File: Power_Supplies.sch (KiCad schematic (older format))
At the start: 70 parts

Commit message: Rick's changes - April 19
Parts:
- removed L?: L_22uH_2.6A_42mOhm_SMT, F_Inductors:L-Bourns-SRU1048-series, symbol OpenVent:L_22uH_2.6A_42mOhm_SMT
- added L?: L_22uH_2.6A_42mOhm_SMT, F_Inductors:L-Bourns-SRU1048-series, symbol OpenVent:L_22uH_2.6A_42mOhm_SMT
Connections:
- net +5V: now also L?.2; no longer L?.1
- net FAN_DRIVE: now also J?.3 (Pin_3); no longer J?.4 (Pin_4)
- net GND: now also D?.2 (CATHODE)
- net PWR_EN: no longer U?.5 (EN)
- net VBUS: now also J?.4 (Pin_4); no longer J?.3 (Pin_3)
- net VDC: now also D2.1 (ANODE), D?.1 (ANODE)
- net V_MAIN: now also L?.2
- net at D2.2 (CATHODE): now also R?.2
- net at D?.1 (ANODE): now also R?.2
- net at C?.1, C?.1, FB?.2: now also L?.1; no longer L?.2
- net at C?.1, C?.1, FB?.2: now also L?.1
- net at R?.1: now also D?.2 (CATHODE)
- net VIN_FAIL_FPGA renamed VIN_FAIL_F
- net VIN_FAIL_MCU renamed VIN_FAIL_M
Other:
- note added: "Add 5V Sensor Power Supply"
- note added: "Add Power Supervisor\nto 7.5V_IN to enable\nlinear regulators"
- note removed: "(Use only for status check of external power supply.)"
- note removed: "(VIN_LIMITED is connected to input 12V through a 1K resistor.)"
- note removed: "Add 5V Sensor Power \nSupply with prefiltering"
- note removed: "FAN DRIVE NEEDS TO BE GENERATED BY FPGA - ANY VOLTAGE\n"
- note removed: "SW_HOME, SW_END, SW_BACKUP\nare off-board microswitches"
- note removed: "Swap VBATT and FAN_DRIVE here and Power board to \nprevent serious damage if cable is installed backwards"
- moved on the sheet: C?, D2, D?, FB?, L?, M?, Q?, R14, R?, U?

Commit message: Annotation has been done
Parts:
- gave numbers to parts that had none: 66
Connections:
- net VMEM: now also D17.6 (K1;A2); no longer D17.3 (A3;K4)
- net V_MAIN: now also D16.3 (A3;K4); no longer D16.6 (K1;A2)
- net at C103.2, U23.4 (VIN), U23.5 (EN): now also D16.5 (K3), D17.2 (K2); no longer D16.2 (K2), D17.5 (K3)

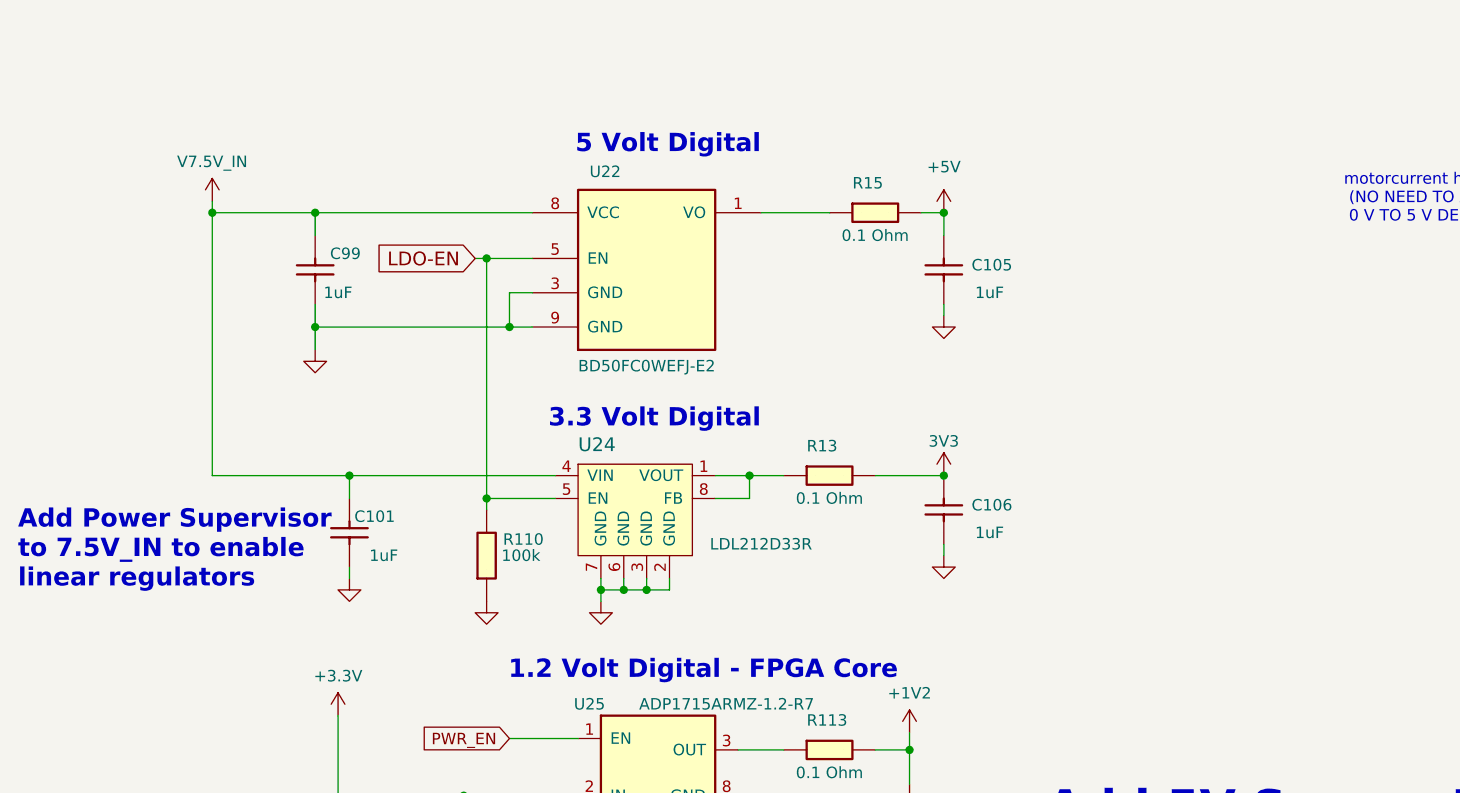
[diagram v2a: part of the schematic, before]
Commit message: Update Power_Supplies.sch
PoR for 7.5V added
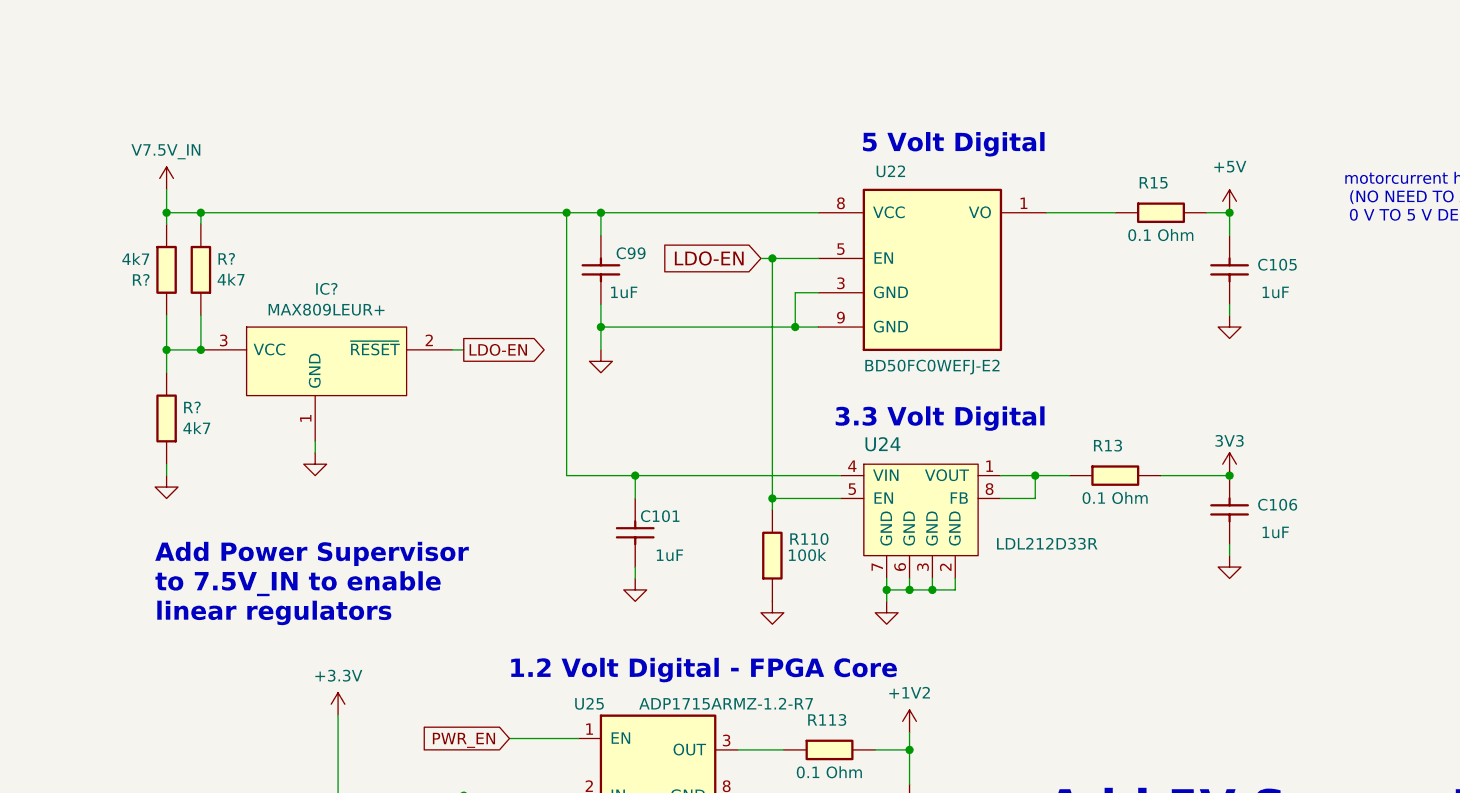
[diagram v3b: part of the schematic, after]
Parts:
- added IC?: MAX809LEUR+, SOT95P237X112-3N, symbol OpenVent:MAX809LEUR+
- added R? (x3): 4.7K_±0.1%_1_6W_±25ppm_℃_0603_High_Precision_&_Lo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, symbol OpenVent:4.7K_±0.1%_1_6W_±25ppm_℃_0603_High_Precision_&_Low_TCR_SMD_Resistors_R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
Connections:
- net +5V: now also R?.1, R?.2
- net GND: now also IC?.1 (GND), R?.1
- net LDO-EN: now also IC?.2 (~RESET)
- new net: IC?.3 (VCC), R?.1, R?.2, R?.2
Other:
- moved on the sheet: C101, C105, C106, C99, R110, R13, R15, U22, U24

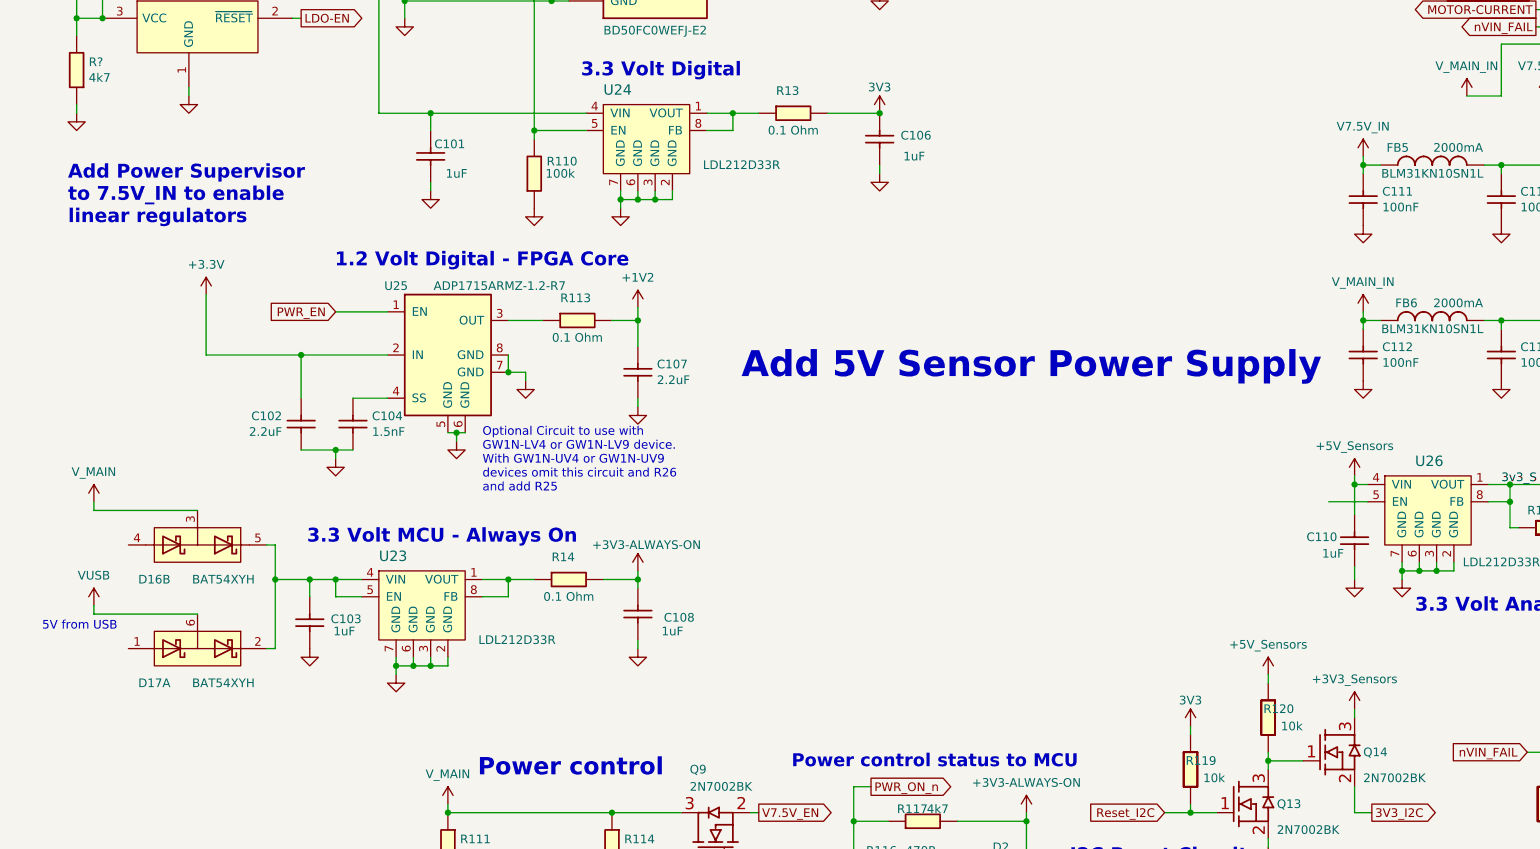
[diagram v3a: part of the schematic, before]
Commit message: Update Power_Supplies.sch
5V analog added
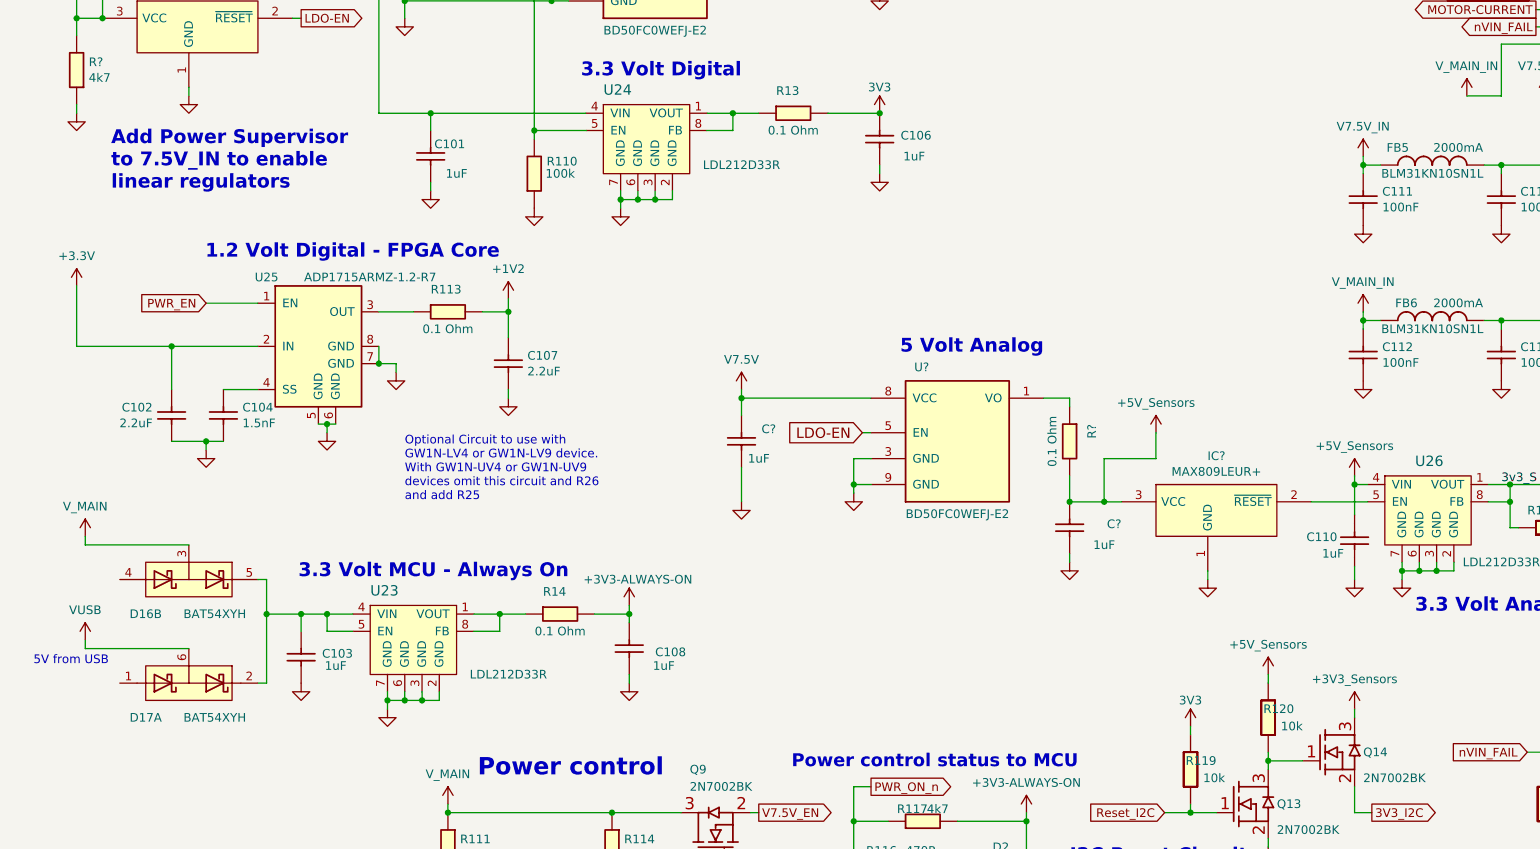
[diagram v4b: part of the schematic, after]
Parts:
- added C? (x2): 1uF_0603_Ceramic_Capacitor,_10%,_50V,_X5R, Capacitor_SMD:C_0603_1608Metric, symbol OpenVent:1uF_0603_Ceramic_Capacitor,_10%,_50V,_X5R
- added IC?: MAX809LEUR+, SOT95P237X112-3N, symbol OpenVent:MAX809LEUR+
- added R?: 0R1_0603_Chip_Resistor,_1%,_0.1W, Resistor_SMD:R_0603_1608Metric, symbol OpenVent:0R1_0603_Chip_Resistor,_1%,_0.1W
- added U?: BD50FC0WEFJ-E2, Package_SO:HSOP-8-1EP_3.9x4.9mm_P1.27mm_EP2.41x3.1mm_ThermalVias, symbol OpenVent:BD50FC0WEFJ-E2
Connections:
- net +5V: now also C?.2, C?.2, IC?.3 (VCC), R?.2, U?.8 (VCC)
- net GND: now also C?.1, C?.1, IC?.1 (GND), U?.3 (GND), U?.9 (GND)
- net LDO-EN: now also U?.5 (EN)
- net at U26.5 (EN): now also IC?.2 (~RESET)
- new net: R?.1, U?.1 (VO)
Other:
- note added: "5 Volt Analog"
- note removed: "Add 5V Sensor Power Supply"
- moved on the sheet: C102, C103, C104, C107, C108, D16B, D17A, R113, R14, U23, U25

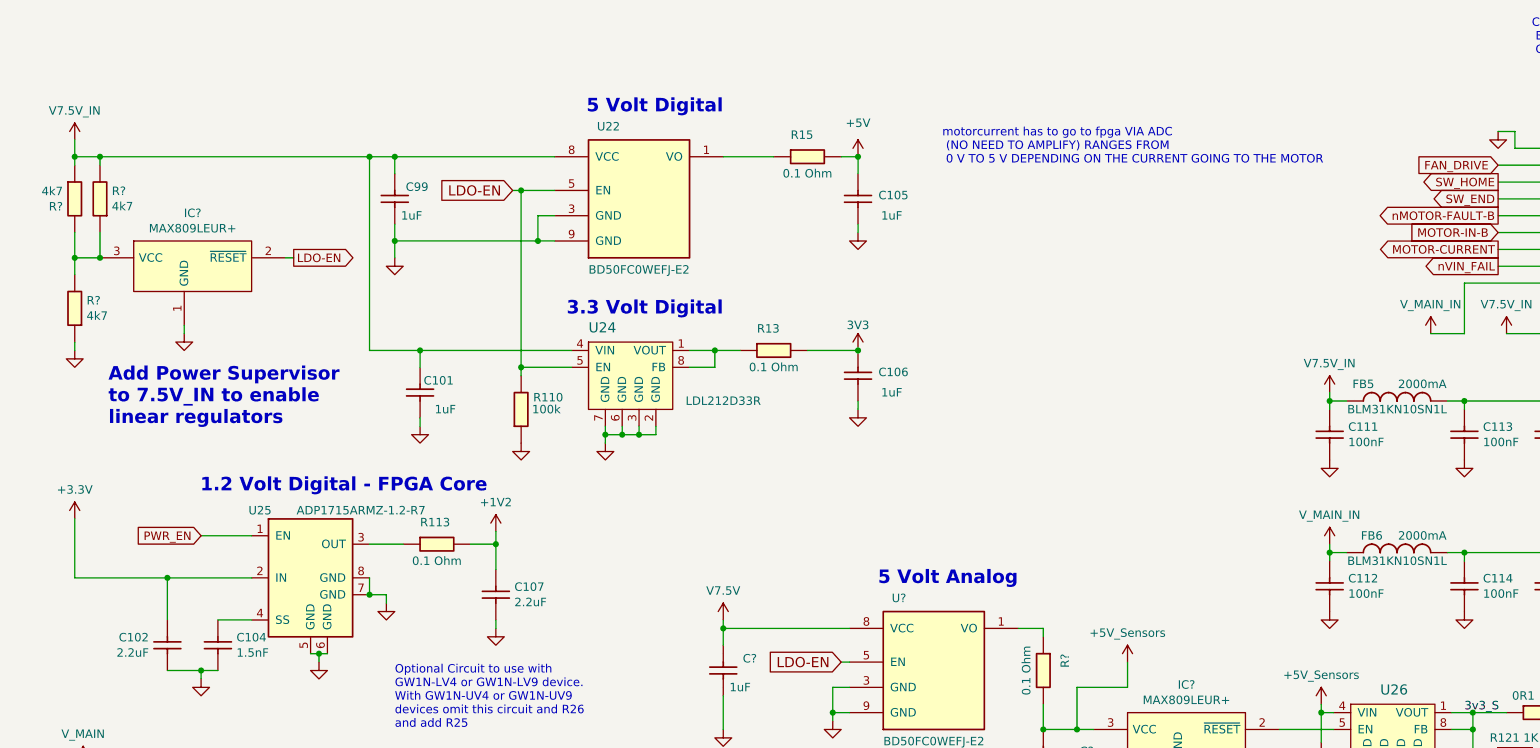
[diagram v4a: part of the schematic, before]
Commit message: Update Power_Supplies.sch
3.3v regulator with soft-start added
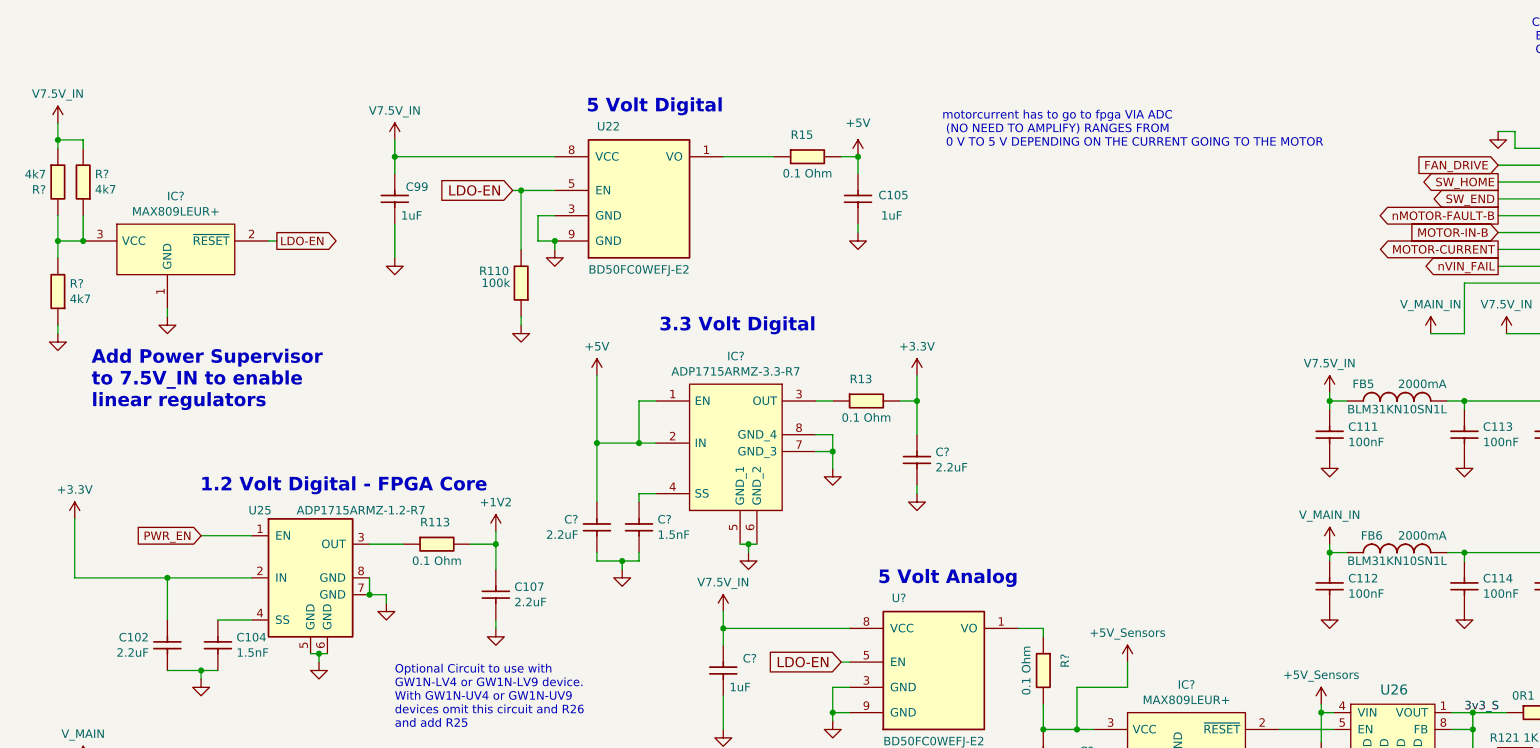
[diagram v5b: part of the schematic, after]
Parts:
- removed C101, C106: 1uF_0603_Ceramic_Capacitor,_10%,_50V,_X5R, Capacitor_SMD:C_0603_1608Metric, symbol OpenVent:1uF_0603_Ceramic_Capacitor,_10%,_50V,_X5R
- removed U24: LDL212D33R, Package_SO:SO-8_5.3x6.2mm_P1.27mm, symbol OpenVent:LDL212D33R
- added C? (x2): 2.2uF_0603_Ceramic_Capacitor,_10%,_50V,_X5R, symbol OpenVent:2.2uF_0603_Ceramic_Capacitor,_10%,_50V,_X5R
- added C?: 1.5nF_0603_Ceramic_Capacitor,_10%,_X7R,_25V, symbol OpenVent:1.5nF_0603_Ceramic_Capacitor,_10%,_X7R,_25V
- added IC?: ADP1715ARMZ-3.3-R7, SOP65P490X110-8N, symbol OpenVent:ADP1715ARMZ-3.3-R7
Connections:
- net +3V3: now also C?.1
- net +5V: now also C?.1, IC?.1 (EN), IC?.2 (IN)
- net GND: now also C?.2, C?.2, C?.2, IC?.5 (GND_1), IC?.6 (GND_2), IC?.7 (GND_3), IC?.8 (GND_4)
- net at R13.1: now also IC?.3 (OUT)
- new net: C?.1, IC?.4 (SS)
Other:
- moved on the sheet: IC?, R110, R13, R?

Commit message: Update Power_Supplies.sch
3.3v regulator changed
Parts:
- removed C? (x2): 2.2uF_0603_Ceramic_Capacitor,_10%,_50V,_X5R, symbol OpenVent:2.2uF_0603_Ceramic_Capacitor,_10%,_50V,_X5R
- removed C?: 1.5nF_0603_Ceramic_Capacitor,_10%,_X7R,_25V, symbol OpenVent:1.5nF_0603_Ceramic_Capacitor,_10%,_X7R,_25V
- removed IC?: ADP1715ARMZ-3.3-R7, SOP65P490X110-8N, symbol OpenVent:ADP1715ARMZ-3.3-R7
- added 1.15K: ERA3AEB1151V, ERA3AEB101V, symbol OpenVent:ERA3AEB1151V
- added 3.57K: ERA3AEB3571V, ERA3AEB101V, symbol OpenVent:ERA3AEB3571V
- added 4.7uF: C3216X5R1H475K085AB, CAPC3216X100N, symbol OpenVent:C3216X5R1H475K085AB
- added 560pF: 06035C561JAT2A, CAPC1608X90N, symbol OpenVent:06035C561JAT2A
- added C?: 2.2uF_0603_Ceramic_Capacitor,_10%,_50V,_X5R, Capacitor_SMD:C_0603_1608Metric, symbol OpenVent:2.2uF_0603_Ceramic_Capacitor,_10%,_50V,_X5R
- added IC?: TPS74801TDRCRQ1, TPS74901DRCR, symbol OpenVent:TPS74801TDRCRQ1
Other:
- moved on the sheet: R13

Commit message: Update Power_Supplies.sch
Regulators 3.3v Digital , 3.3 Analog and 1.2v added with soft-start and PG for Config_n signal (FPGA)
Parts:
- removed 1.15K: ERA3AEB1151V, ERA3AEB101V, symbol OpenVent:ERA3AEB1151V
- removed 3.57K: ERA3AEB3571V, ERA3AEB101V, symbol OpenVent:ERA3AEB3571V
- removed C102: 2.2uF_0603_Ceramic_Capacitor,_10%,_50V,_X5R, symbol OpenVent:2.2uF_0603_Ceramic_Capacitor,_10%,_50V,_X5R
- removed C104: 1.5nF_0603_Ceramic_Capacitor,_10%,_X7R,_25V, symbol OpenVent:1.5nF_0603_Ceramic_Capacitor,_10%,_X7R,_25V
- removed C110, C117: 1uF_0603_Ceramic_Capacitor,_10%,_50V,_X5R, Capacitor_SMD:C_0603_1608Metric, symbol OpenVent:1uF_0603_Ceramic_Capacitor,_10%,_50V,_X5R
- removed C?: 2.2uF_0603_Ceramic_Capacitor,_10%,_50V,_X5R, Capacitor_SMD:C_0603_1608Metric, symbol OpenVent:2.2uF_0603_Ceramic_Capacitor,_10%,_50V,_X5R
- removed IC?: MAX809LEUR+, SOT95P237X112-3N, symbol OpenVent:MAX809LEUR+
- removed IC?: TPS74801TDRCRQ1, TPS74901DRCR, symbol OpenVent:TPS74801TDRCRQ1
- removed R122: 0R1_0603_Chip_Resistor,_1%,_0.1W, Resistor_SMD:R_0603_1608Metric, symbol OpenVent:0R1_0603_Chip_Resistor,_1%,_0.1W
- removed U25: ADP1715ARMZ-1.2-R7, symbol OpenVent:ADP1715ARMZ-1.2-R7
- removed U26: LDL212D33R, Package_SO:SO-8_5.3x6.2mm_P1.27mm, symbol OpenVent:LDL212D33R
- added 2.49K: ERA3AEB2491V, ERA3AEB101V, symbol OpenVent:ERA3AEB2491V
- added 4.99K: ERA3AEB4991V, ERA3AEB101V, symbol OpenVent:ERA3AEB4991V
- added C? (x4): 2.2uF_0603_Ceramic_Capacitor,_10%,_50V,_X5R, Capacitor_SMD:C_0603_1608Metric, symbol OpenVent:2.2uF_0603_Ceramic_Capacitor,_10%,_50V,_X5R
- added C? (x2): 1.5nF_0603_Ceramic_Capacitor,_10%,_X7R,_25V, symbol OpenVent:1.5nF_0603_Ceramic_Capacitor,_10%,_X7R,_25V
- added IC?: TPS74801TDRCRQ1, TPS74901DRCR, symbol OpenVent:TPS74801TDRCRQ1
- added IC? (x2): ADP1715ARMZ-3.3-R7, SOP65P490X110-8N, symbol OpenVent:ADP1715ARMZ-3.3-R7
- added R?: 0R1_0603_Chip_Resistor,_1%,_0.1W, Resistor_SMD:R_0603_1608Metric, symbol OpenVent:0R1_0603_Chip_Resistor,_1%,_0.1W
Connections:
- net labels added: CONFIG_N
- net labels removed: 3v3_S
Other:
- note added: "2 square inches of copper on\neach side of the board for\nheat sinking for 5V\nDigital Regulator"
- note added: "3.3v Digital, 3.3v Analog and 1.2v regulators with soft-start (ramp for FPGA)"
- note removed: "Add Power Supervisor\nto 7.5V_IN to enable\nlinear regulators"
- note removed: "Optional Circuit to use with\nGW1N-LV4 or GW1N-LV9 device. \nWith GW1N-UV4 or GW1N-UV9 \ndevices omit this circuit and R26 \nand add R25"
- moved on the sheet: C105, C107, C?, D18, R113, R121, R13, R15, R?, U?
